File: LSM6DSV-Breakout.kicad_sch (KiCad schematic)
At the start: 16 parts, among them CN1 AFC10-S04QCA-00, CN2 AFC10-S04QCA-00, J1 Conn_01x06_Pin, J2 Conn_01x04_Pin, U1 LSM6DSVTR

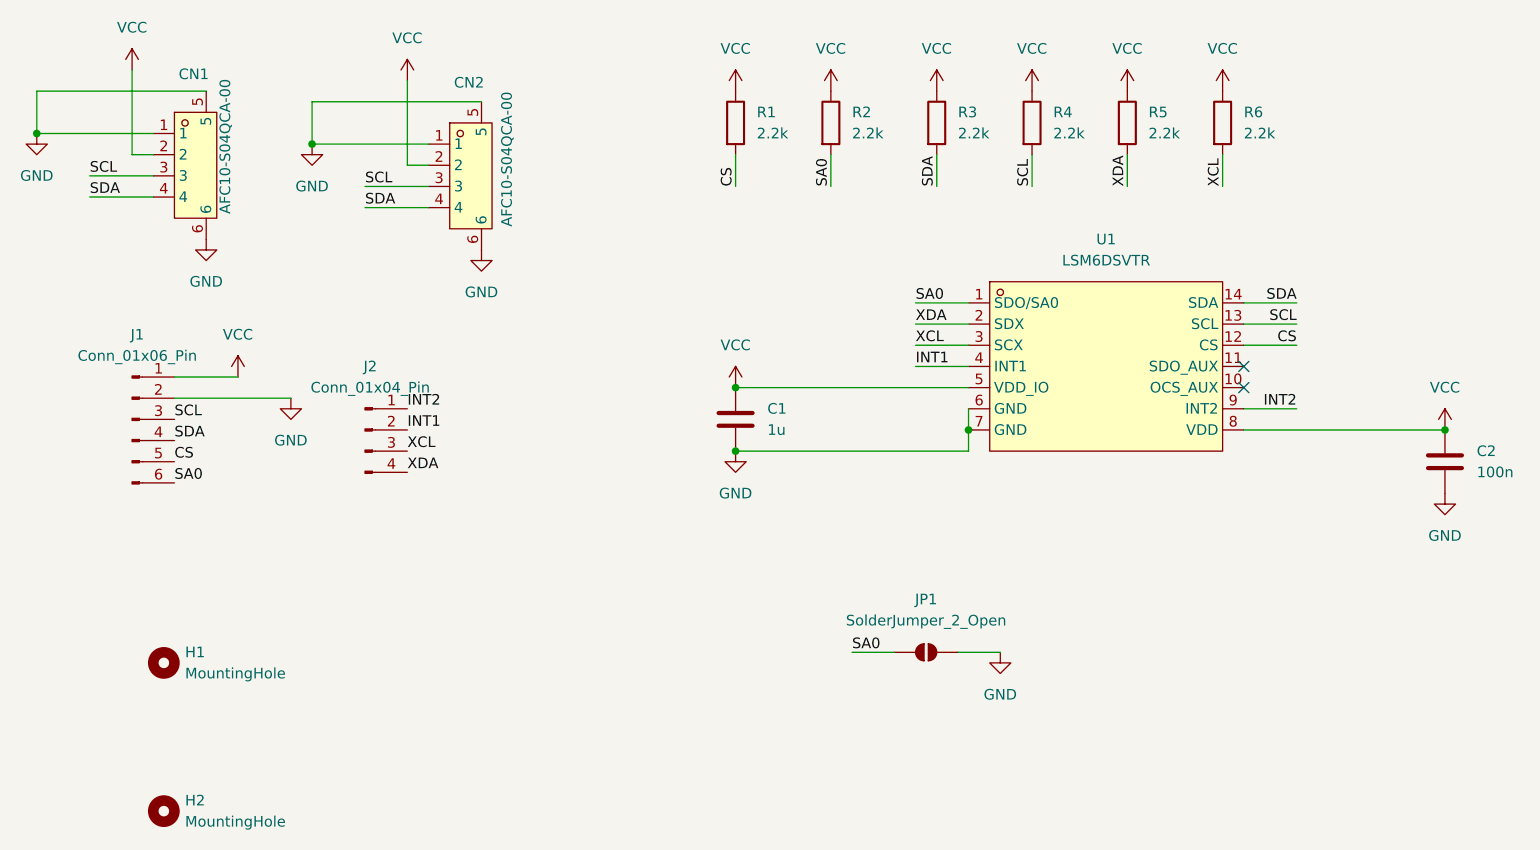
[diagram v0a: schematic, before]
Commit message: Unified 6DoF IMU footprint
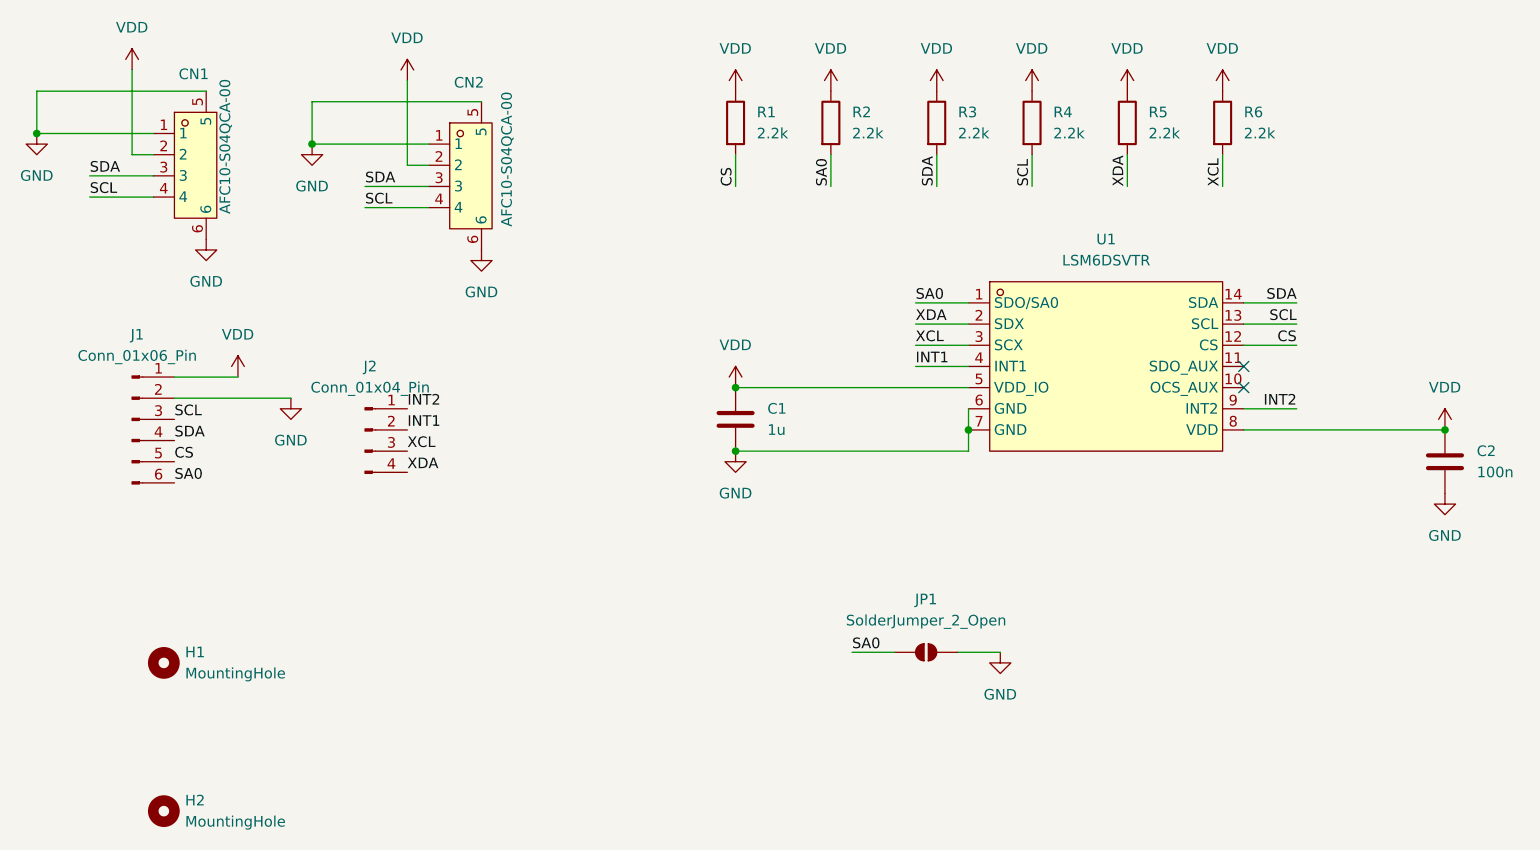
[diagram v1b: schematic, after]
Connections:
- net SCL: now also CN1.4, CN2.4; no longer CN1.3, CN2.3
- net SDA: now also CN1.3, CN2.3; no longer CN1.4, CN2.4
- net VCC renamed VDD

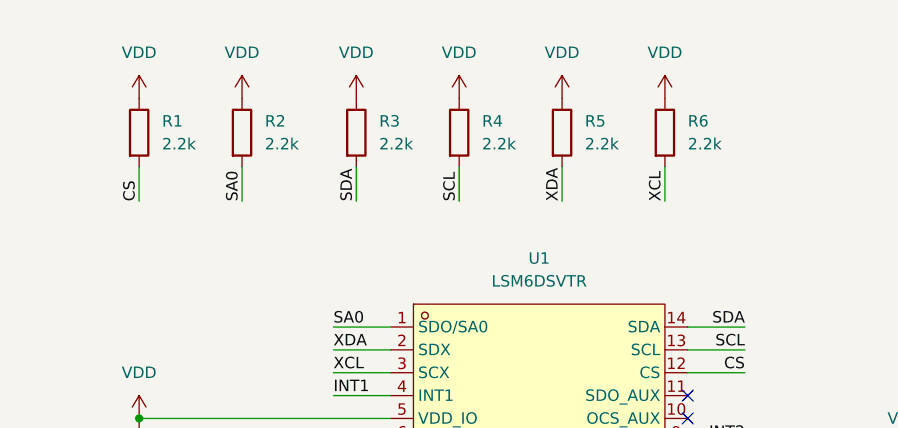
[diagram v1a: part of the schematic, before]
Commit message: use higher pullup, make dippable
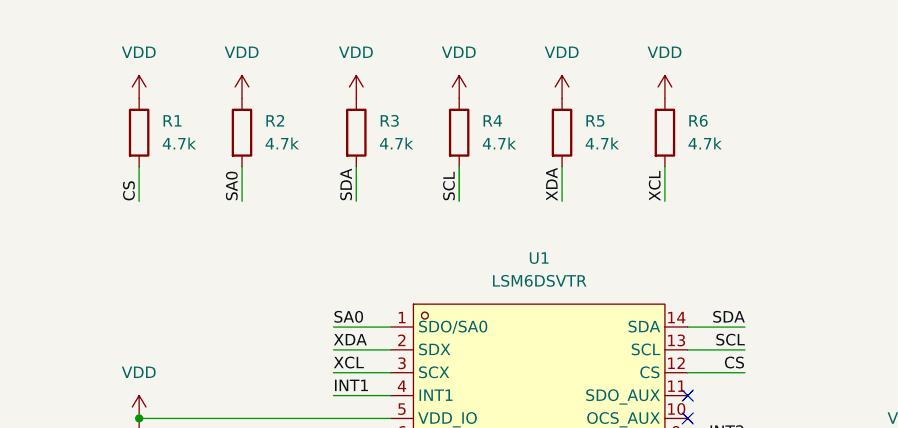
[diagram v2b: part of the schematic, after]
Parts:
- R1, R2, R3, R4, R5, R6: value 2.2k -> 4.7k
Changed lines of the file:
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@@
 			)
 		)
-		(property "Value" "2.2k"
+		(property "Value" "4.7k"
 			(at 161.29 26.6699 0)
 			(effects
@@
 			)
 		)
-		(property "Value" "2.2k"
+		(property "Value" "4.7k"
 			(at 114.3 26.6699 0)
 			(effects
@@
 			)
 		)
-		(property "Value" "2.2k"
+		(property "Value" "4.7k"
 			(at 102.87 26.6699 0)
 			(effects
@@
 			)
 		)
-		(property "Value" "2.2k"
+		(property "Value" "4.7k"
 			(at 138.43 26.6699 0)
 			(effects
@@
 			)
 		)
-		(property "Value" "2.2k"
+		(property "Value" "4.7k"
 			(at 149.86 26.6699 0)
 			(effects
@@
 			)
 		)
-		(property "Value" "2.2k"
+		(property "Value" "4.7k"
 			(at 127 26.6699 0)
 			(effects
